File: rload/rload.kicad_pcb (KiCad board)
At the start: 2 copper layers, 100 x 86 mm, 56 parts, among them J1 Conn_01x01, J2 Conn_01x01, J3 AVR-ISP-6, J4 Barrel_Jack_Switch, J5 Conn_02x05_Odd_Even, J6 Conn_01x01, J7 Conn_01x01, J8 USB_B_Micro, Q1 Q_NMOS_GDS, SW1 SW_Push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

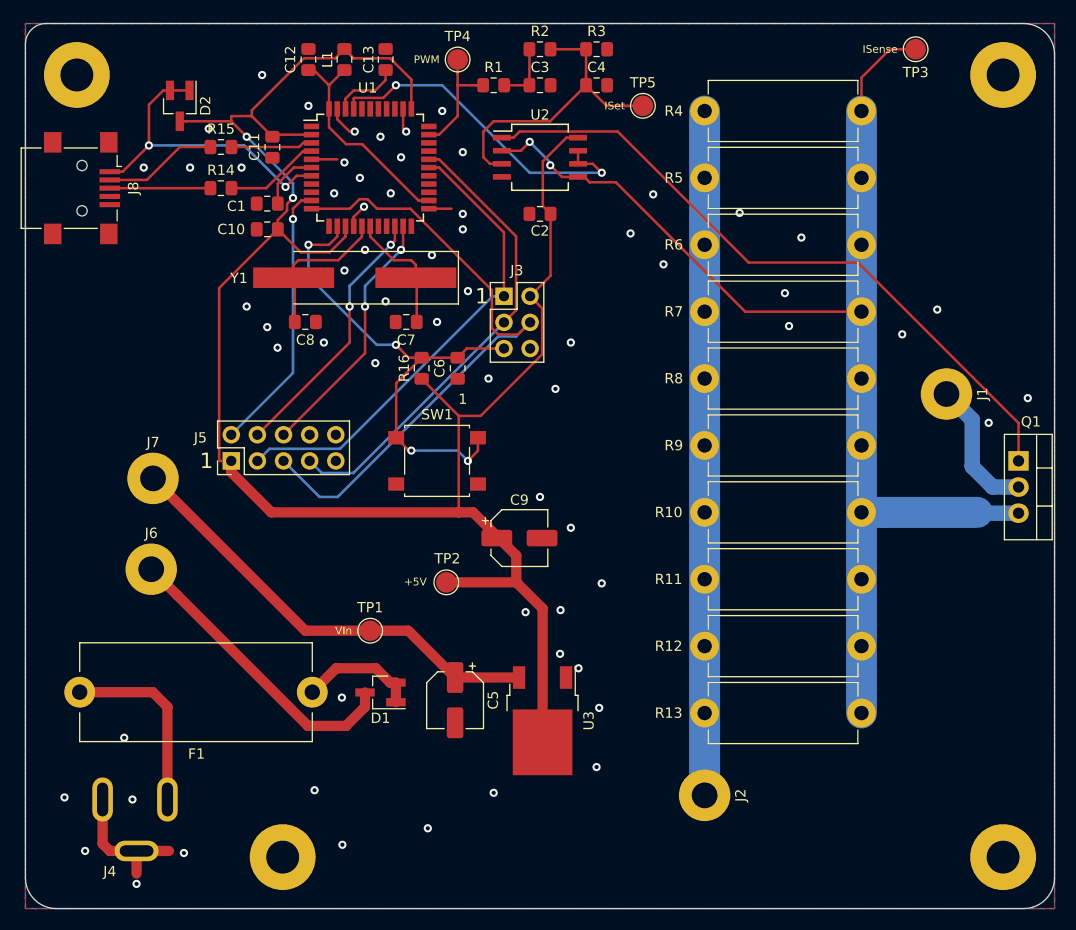
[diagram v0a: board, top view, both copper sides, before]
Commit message: Add python script to generate a svg of a pcb
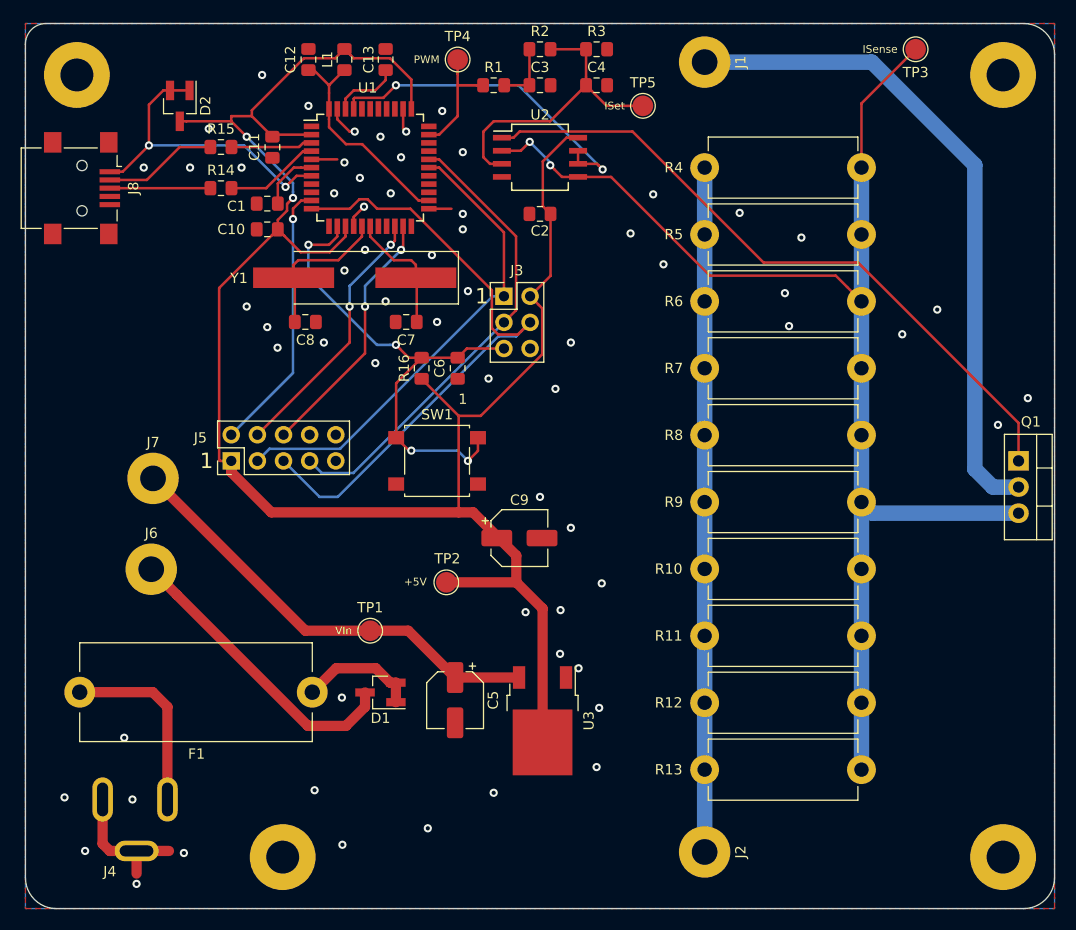
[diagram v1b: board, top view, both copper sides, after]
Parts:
- moved J1 39.9 mm to (134.0, 46.8)
- moved J2 5.50 mm to (134.0, 123.5)
- moved R10 5.50 mm to (134.0, 96.0)
- moved R11 5.50 mm to (134.0, 102.5)
- moved R12 5.50 mm to (134.0, 109.0)
- moved R13 5.50 mm to (134.0, 115.5)
- moved R4 5.50 mm to (134.0, 57.0)
- moved R5 5.50 mm to (134.0, 63.5)
- moved R6 5.50 mm to (134.0, 70.0)
- moved R7 5.50 mm to (134.0, 76.5)
- moved R8 5.50 mm to (134.0, 83.0)
- moved R9 5.50 mm to (134.0, 89.5)
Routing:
- net Net-(J1-Pad1): track 13.4 -> 64.9 mm
- net I_SENSE: track 125.7 -> 129.8 mm
